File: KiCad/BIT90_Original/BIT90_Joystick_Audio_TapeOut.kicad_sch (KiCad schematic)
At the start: 21 parts, among them U10 74LS04, U11 74LS138, U12 74LS00, U14 74LS05, U25 LM393, U33 74LS244, U34 74LS244, U6 SN76489AN, U9 74LS00

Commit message: Minor schematic corrections
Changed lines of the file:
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@@
 		(company "Brett Hallen")
 		(comment 3 "From Sheet 6-3")
-		(comment 4 "Based on original schematics from BIT Corporation")
+		(comment 4 "Based on original schematics from BIT Corporation (普澤有限公司)")
 	)
 	(text_box "I don't understand this:\nU12 pin 12 input connected to U10 pin 13 input ... ?"
@@
 	)
 	(global_label "AUDIO OUT"
-		(shape input)
+		(shape output)
 		(at 57.15 40.64 180)
 		(fields_autoplaced yes)

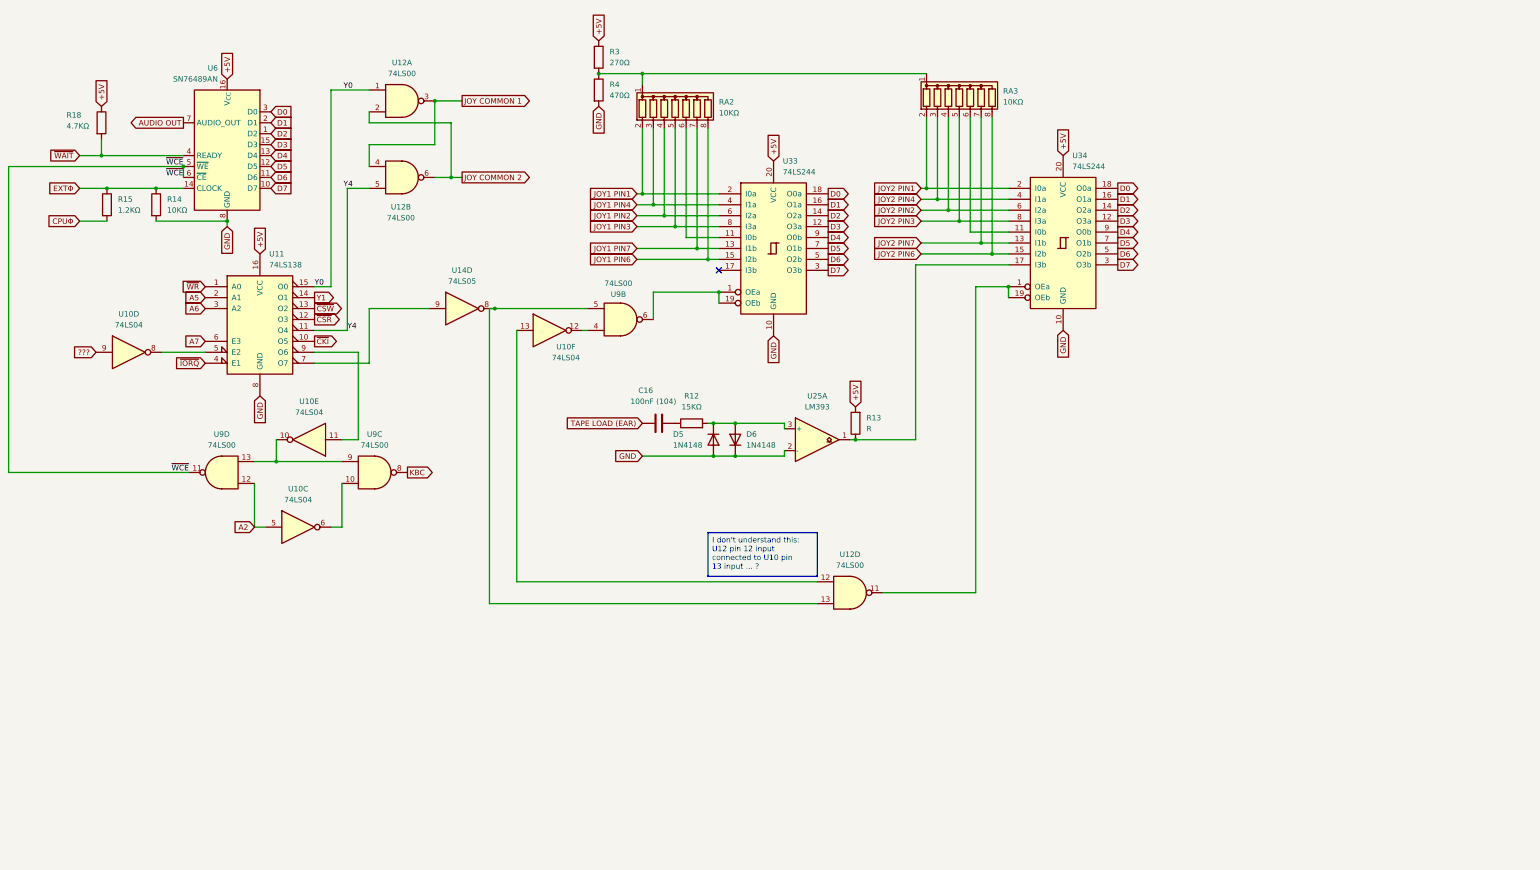
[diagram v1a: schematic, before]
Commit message: Completed original schematic redraw
Well, didn't finish the Video Encoder (PAL) sheet as I'm not going to use any of it in the new design.
Moved the audio output from that sheet to the Joystick/Audio/Tape out sheet where the sound generator is.
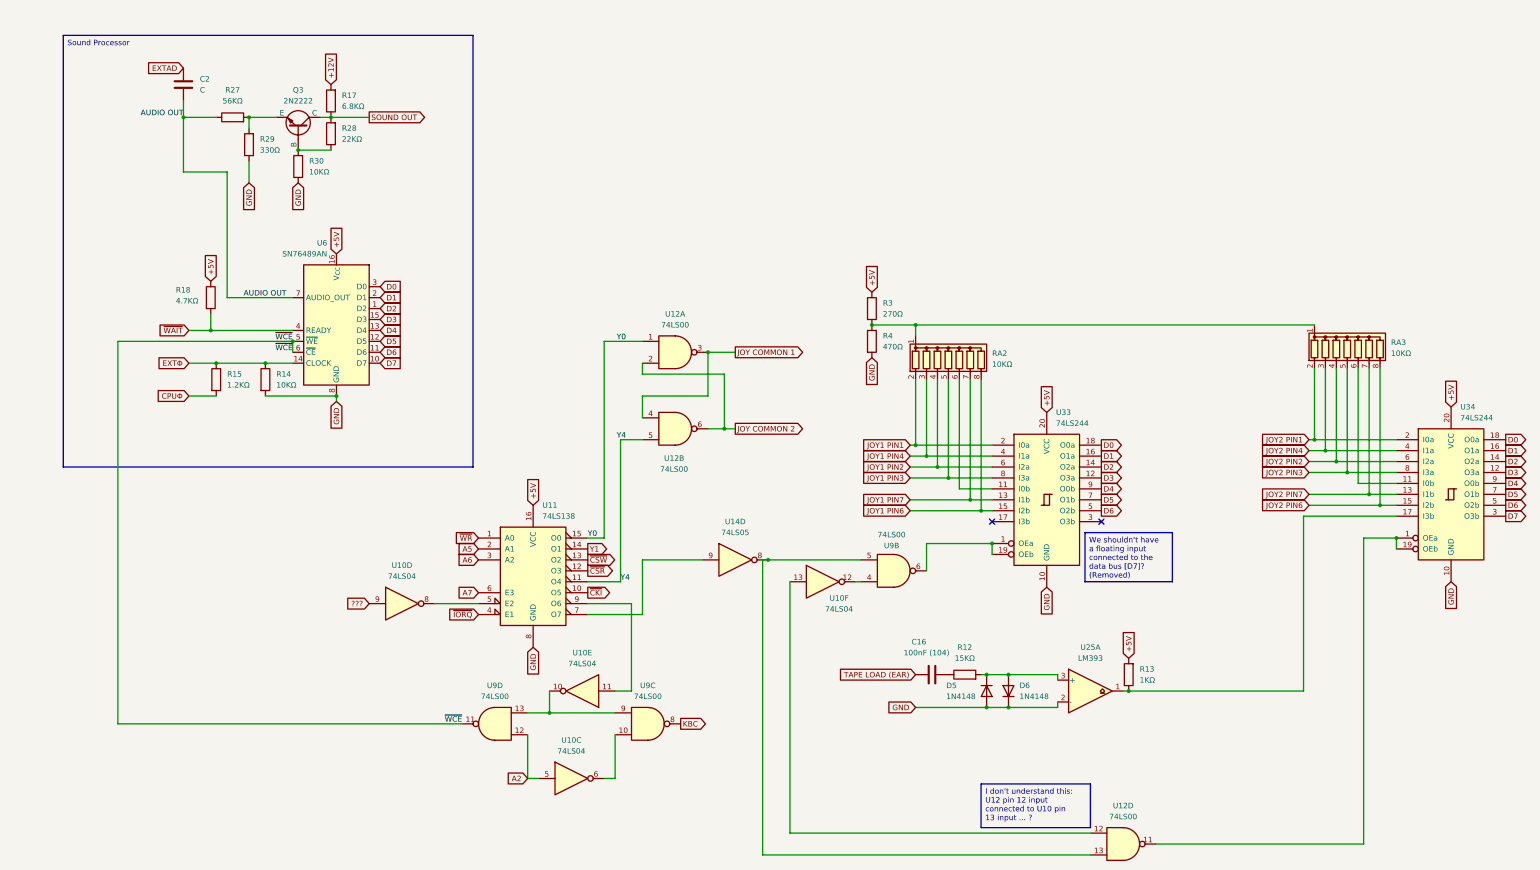
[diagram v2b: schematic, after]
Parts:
- added C2: C, symbol Device:C
- added Q3: 2N2222, symbol Simulation_SPICE:NPN
- added R17: 6.8KΩ, symbol Device:R
- added R27: 56KΩ, symbol Device:R
- added R28: 22KΩ, symbol Device:R
- added R29: 330Ω, symbol Device:R
- added R30: 10KΩ, symbol Device:R
- R13: value R -> 1KΩ
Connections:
- net AUDIO OUT: now also C2.2, R27.1
- net D7: no longer U33.3 (O3b)
- net GND: now also R29.1, R30.1
- new net: Q3.3 (E), R27.2, R29.2
- new net: Q3.2 (B), R28.1, R30.2
- new net +12V: R17.2
- new net EXTAD: C2.1
- new net SOUND OUT: Q3.1 (C), R17.1, R28.2
- no-connect marks 1 -> 2
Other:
- moved on the sheet: C16, D5, D6, R12, R13, R14, R15, R18, R3, R4, RA2, RA3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

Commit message: Small updates/corrections
Managed to figure out some more errors/missing info from ColecoVision schematics & Henk's BIT90 motherboard underside photo
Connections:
- net D7: now also U33.3 (O3b)
- net A1: now reaches U10.13, U12.12
- net ??? renamed ~{DISM}
- net JOY COMMON 1 renamed CTRL COMMON 1
- net JOY COMMON 2 renamed CTRL COMMON 2
- net JOY1 PIN1 renamed CTRL1 PIN1
- net JOY1 PIN2 renamed CTRL1 PIN2
- net JOY1 PIN3 renamed CTRL1 PIN3
- net JOY1 PIN4 renamed CTRL1 PIN4
- net JOY1 PIN6 renamed CTRL1 PIN6
- net JOY1 PIN7 renamed CTRL1 PIN7
- net JOY2 PIN1 renamed CTRL2 PIN1
- net JOY2 PIN2 renamed CTRL2 PIN2
- net JOY2 PIN3 renamed CTRL2 PIN3
- net JOY2 PIN4 renamed CTRL2 PIN4
- net JOY2 PIN6 renamed CTRL2 PIN6
- net JOY2 PIN7 renamed CTRL2 PIN7
- no-connect marks 2 -> 1
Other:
- moved on the sheet: U10F, U12D, U9B
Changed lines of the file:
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@@
 	(title_block
 		(title "BIT90 Joystick, Audio, Tape Out")
-		(date "3/JUN/2026")
+		(date "5/JUN/2026")
 		(rev "A")
 		(company "Brett Hallen")
@@
 		(comment 4 "Based on original schematics from BIT Corporation (普澤有限公司)")
 	)
-	(text_box "I don't understand this:\nU12 pin 12 input connected to U10 pin 13 input ... ?"
+	(text_box "Sound Processor"
 		(exclude_from_sim no)
-		(at 242.57 194.31 0)
-		(size 25.4 10.16)
+		(at 29.21 20.32 0)
+		(size 95.25 100.33)
 		(margins 0.9525 0.9525 0.9525 0.9525)
 		(stroke
@@
 		)
 	)
-	(text_box "Sound Processor"
+	(text_box "We shouldn't have a floating input connected to the data bus [D7]?"
 		(exclude_from_sim no)
-		(at 29.21 20.32 0)
-		(size 95.25 100.33)
+		(at 267.97 137.16 0)
+		(size 20.32 10.16)
 		(margins 0.9525 0.9525 0.9525 0.9525)
 		(stroke
@@
 		)
 	)
-	(text_box "We shouldn't have a floating input connected to the data bus [D7]? (Removed)"
+	(text_box "Inverter input is unlabelled on the original BIT90 schematic.\nIt comes from pin 29 on the expansion connector in the ColecoVision so assuming same here "
 		(exclude_from_sim no)
-		(at 266.7 135.89 0)
-		(size 20.32 11.43)
+		(at 66.04 154.94 0)
+		(size 34.29 15.24)
 		(margins 0.9525 0.9525 0.9525 0.9525)
 		(stroke
@@
 		(at 245.11 133.35)
 	)
-	(no_connect
-		(at 270.51 133.35)
-	)
 	(wire
 		(pts
-			(xy 245.11 138.43) (xy 229.87 138.43)
+			(xy 245.11 138.43) (xy 233.68 138.43)
 		)
 		(stroke
@@
 	(wire
 		(pts
-			(xy 331.47 208.28) (xy 283.21 208.28)
+			(xy 331.47 191.77) (xy 237.49 191.77)
 		)
 		(stroke
@@
 	(wire
 		(pts
-			(xy 331.47 208.28) (xy 331.47 137.16)
+			(xy 331.47 191.77) (xy 331.47 137.16)
 		)
 		(stroke
@@
 	(wire
 		(pts
-			(xy 213.36 147.32) (xy 214.63 147.32)
-		)
-		(stroke
-			(width 0)
-			(type default)
-		)
-	)
-	(wire
-		(pts
 			(xy 58.42 96.52) (xy 64.77 96.52)
 		)
@@
 	(wire
 		(pts
-			(xy 267.97 210.82) (xy 191.77 210.82)
+			(xy 222.25 194.31) (xy 193.04 194.31)
 		)
 		(stroke
@@
 	(wire
 		(pts
-			(xy 229.87 138.43) (xy 229.87 144.78)
+			(xy 233.68 138.43) (xy 233.68 144.78)
 		)
 		(stroke
@@
 	(wire
 		(pts
-			(xy 193.04 142.24) (xy 214.63 142.24)
+			(xy 193.04 142.24) (xy 218.44 142.24)
 		)
 		(stroke
@@
 	(wire
 		(pts
-			(xy 198.12 147.32) (xy 198.12 205.74)
-		)
-		(stroke
-			(width 0)
-			(type default)
-		)
-	)
-	(wire
-		(pts
 			(xy 63.5 88.9) (xy 82.55 88.9)
 		)
@@
 	(wire
 		(pts
-			(xy 191.77 210.82) (xy 191.77 142.24)
+			(xy 193.04 194.31) (xy 193.04 142.24)
 		)
 		(stroke
@@
 	(wire
 		(pts
-			(xy 198.12 205.74) (xy 267.97 205.74)
-		)
-		(stroke
-			(width 0)
-			(type default)
-		)
-	)
-	(wire
-		(pts
-			(xy 193.04 142.24) (xy 191.77 142.24)
-		)
-		(stroke
-			(width 0)
-			(type default)
-		)
-	)
-	(wire
-		(pts
 			(xy 234.95 100.33) (xy 234.95 123.19)
 		)
@@
 		)
 	)
-	(global_label "???"
+	(global_label "~{DISM}"
 		(shape input)
 		(at 100.33 152.4 180)
@@
 		)
 		(property "Intersheetrefs" "${INTERSHEET_REFS}"
-			(at 94.079 152.4 0)
+			(at 92.8091 152.4 0)
 			(effects
 				(font
@@
 		)
 	)
-	(global_label "JOY2 PIN7"
+	(global_label "CTRL2 PIN7"
 		(shape input)
 		(at 318.77 127 180)
@@
 		)
 	)
+	(global_label "A1"
+		(shape input)
+		(at 222.25 189.23 180)
+		(fields_autoplaced yes)
+		(effects
+			(font
+				(size 1.27 1.27)
+			)
+			(justify right)
+		)
+		(property "Intersheetrefs" "${INTERSHEET_REFS}"
+			(at 216.9667 189.23 0)
+			(effects
+				(font
+					(size 1.27 1.27)
+				)
+				(justify right)
+				(hide yes)
+			)
+		)
+	)
 	(global_label "D3"
 		(shape output)
@@
 		)
 	)
-	(global_label "JOY1 PIN6"
+	(global_label "CTRL1 PIN6"
 		(shape input)
 		(at 226.06 130.81 180)
@@
 		)
 	)
-	(global_label "JOY1 PIN1"
+	(global_label "CTRL1 PIN1"
 		(shape input)
 		(at 226.06 115.57 180)
@@
 		)
 	)
-	(global_label "JOY2 PIN3"
+	(global_label "CTRL2 PIN3"
 		(shape input)
 		(at 318.77 121.92 180)
@@
 		)
 	)
-	(global_label "JOY2 PIN4"
+	(global_label "CTRL2 PIN4"
 		(shape input)
 		(at 318.77 116.84 180)
@@
 		)
 	)
+	(global_label "A1"
+		(shape input)
+		(at 203.2 147.32 180)
+		(fields_autoplaced yes)
+		(effects
+			(font
+				(size 1.27 1.27)
+			)
+			(justify right)
+		)
+		(property "Intersheetrefs" "${INTERSHEET_REFS}"
+			(at 197.9167 147.32 0)
+			(effects
+				(font
+					(size 1.27 1.27)
+				)
+				(justify right)
+				(hide yes)
+			)
+		)
+	)
 	(global_label "D7"
 		(shape output)
@@
 		)
 	)
-	(global_label "JOY2 PIN2"
+	(global_label "CTRL2 PIN2"
 		(shape input)
 		(at 318.77 119.38 180)
@@
 		)
 	)
-	(global_label "JOY COMMON 1"
+	(global_label "CTRL COMMON 1"
 		(shape output)
 		(at 185.42 93.98 0)
@@
 		)
 	)
-	(global_label "JOY1 PIN7"
+	(global_label "CTRL1 PIN7"
 		(shape input)
 		(at 226.06 128.27 180)
@@
 		)
 	)
-	(global_label "JOY2 PIN6"
+	(global_label "CTRL2 PIN6"
 		(shape input)
 		(at 318.77 129.54 180)
@@
 		)
 	)
+	(global_label "D7"
+		(shape output)
+		(at 270.51 133.35 0)
+		(fields_autoplaced yes)
+		(effects
+			(font
+				(size 1.27 1.27)
+			)
+			(justify left)
+		)
+		(property "Intersheetrefs" "${INTERSHEET_REFS}"
+			(at 275.9747 133.35 0)
+			(effects
+				(font
+					(size 1.27 1.27)
+				)
+				(justify left)
+				(hide yes)
+			)
+		)
+	)
 	(global_label "~{CKI}"
 		(shape output)
@@
 		)
 	)
-	(global_label "JOY1 PIN2"
+	(global_label "CTRL1 PIN2"
 		(shape input)
 		(at 226.06 120.65 180)
@@
 		)
 	)
-	(global_label "JOY COMMON 2"
+	(global_label "CTRL COMMON 2"
 		(shape output)
 		(at 185.42 111.76 0)
@@
 		)
 	)
-	(global_label "JOY2 PIN1"
+	(global_label "CTRL2 PIN1"
 		(shape input)
 		(at 318.77 114.3 180)
@@
 		)
 	)
-	(global_label "JOY1 PIN4"
+	(global_label "CTRL1 PIN4"
 		(shape input)
 		(at 226.06 118.11 180)
@@
 		)
 	)
-	(global_label "JOY1 PIN3"
+	(global_label "CTRL1 PIN3"
 		(shape input)
 		(at 226.06 123.19 180)
@@
 	(symbol
 		(lib_id "74xx:74LS00")
-		(at 275.59 208.28 0)
+		(at 229.87 191.77 0)
 		(unit 4)
 		(exclude_from_sim no)
@@
 		(fields_autoplaced yes)
 		(property "Reference" "U12"
-			(at 275.5817 199.39 0)
+			(at 229.8617 182.88 0)
 			(effects
 				(font
@@
 		)
 		(property "Value" "74LS00"
-			(at 275.5817 201.93 0)
+			(at 229.8617 185.42 0)
 			(effects
 				(font
@@
 		)
 		(property "Footprint" ""
-			(at 275.59 208.28 0)
+			(at 229.87 191.77 0)
 			(effects
 				(font
@@
 		)
 		(property "Datasheet" "http://www.ti.com/lit/gpn/sn74ls00"
-			(at 275.59 208.28 0)
+			(at 229.87 191.77 0)
 			(effects
 				(font
@@
 		)
 		(property "Description" "quad 2-input NAND gate"
-			(at 275.59 208.28 0)
+			(at 229.87 191.77 0)
 			(effects
 				(font
@@
 	(symbol
 		(lib_id "74xx:74LS00")
-		(at 222.25 144.78 0)
+		(at 226.06 144.78 0)
 		(mirror x)
 		(unit 2)
@@
 		(dnp no)
 		(property "Reference" "U9"
-			(at 221.742 138.938 0)
+			(at 225.552 138.938 0)
 			(effects
 				(font
@@
 		)
 		(property "Value" "74LS00"
-			(at 221.742 136.398 0)
+			(at 225.552 136.398 0)
 			(effects
 				(font
@@
 		)
 		(property "Footprint" ""
-			(at 222.25 144.78 0)
+			(at 226.06 144.78 0)
 			(effects
 				(font
@@
 		)
 		(property "Datasheet" "http://www.ti.com/lit/gpn/sn74ls00"
-			(at 222.25 144.78 0)
+			(at 226.06 144.78 0)
 			(effects
 				(font
@@
 		)
 		(property "Description" "quad 2-input NAND gate"
-			(at 222.25 144.78 0)
+			(at 226.06 144.78 0)
 			(effects
 				(font
@@
 	(symbol
 		(lib_id "74xx:74LS04")
-		(at 205.74 147.32 0)
+		(at 210.82 147.32 0)
 		(unit 6)
 		(exclude_from_sim no)
@@
 		(dnp no)
 		(property "Reference" "U10"
-			(at 209.55 151.13 0)
+			(at 214.63 151.13 0)
 			(effects
 				(font
@@
 		)
 		(property "Value" "74LS04"
-			(at 209.55 153.67 0)
+			(at 214.63 153.67 0)
 			(effects
 				(font
@@
 		)
 		(property "Footprint" ""
-			(at 205.74 147.32 0)
+			(at 210.82 147.32 0)
 			(effects
 				(font
@@
 		)
 		(property "Datasheet" "http://www.ti.com/lit/gpn/sn74LS04"
-			(at 205.74 147.32 0)
+			(at 210.82 147.32 0)
 			(effects
 				(font
@@
 		)
 		(property "Description" "Hex Inverter"
-			(at 205.74 147.32 0)
+			(at 210.82 147.32 0)
 			(effects
 				(font

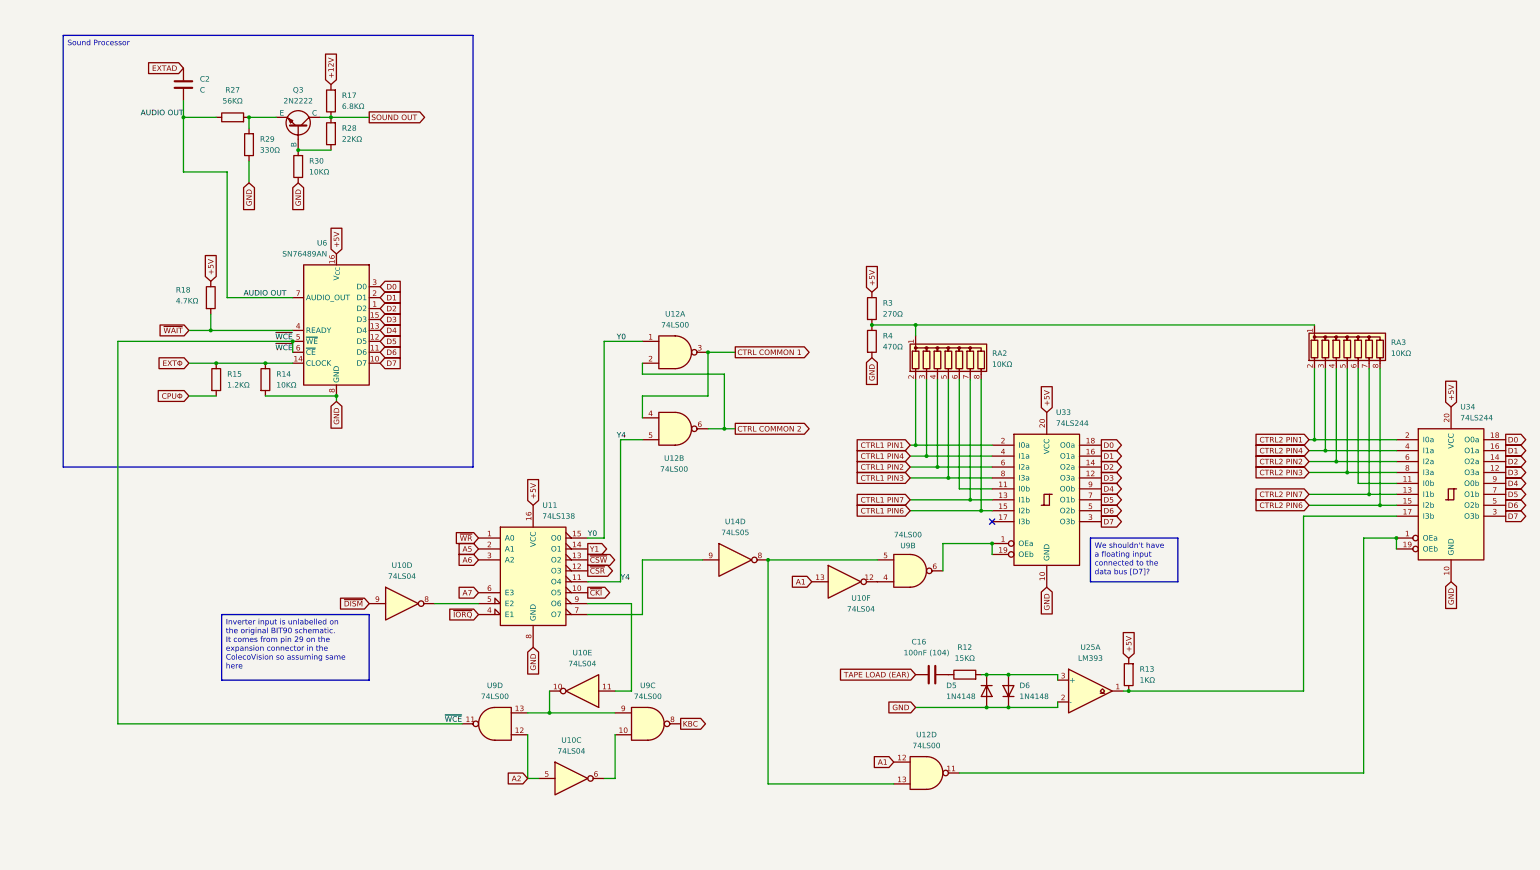
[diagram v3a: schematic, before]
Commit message: Resolved audio clock signal
Marked as EXTΦ on BIT90 schematic, generated via resistor from CPUΦ
Renamed it as AUDΦ so it's a bit clearer
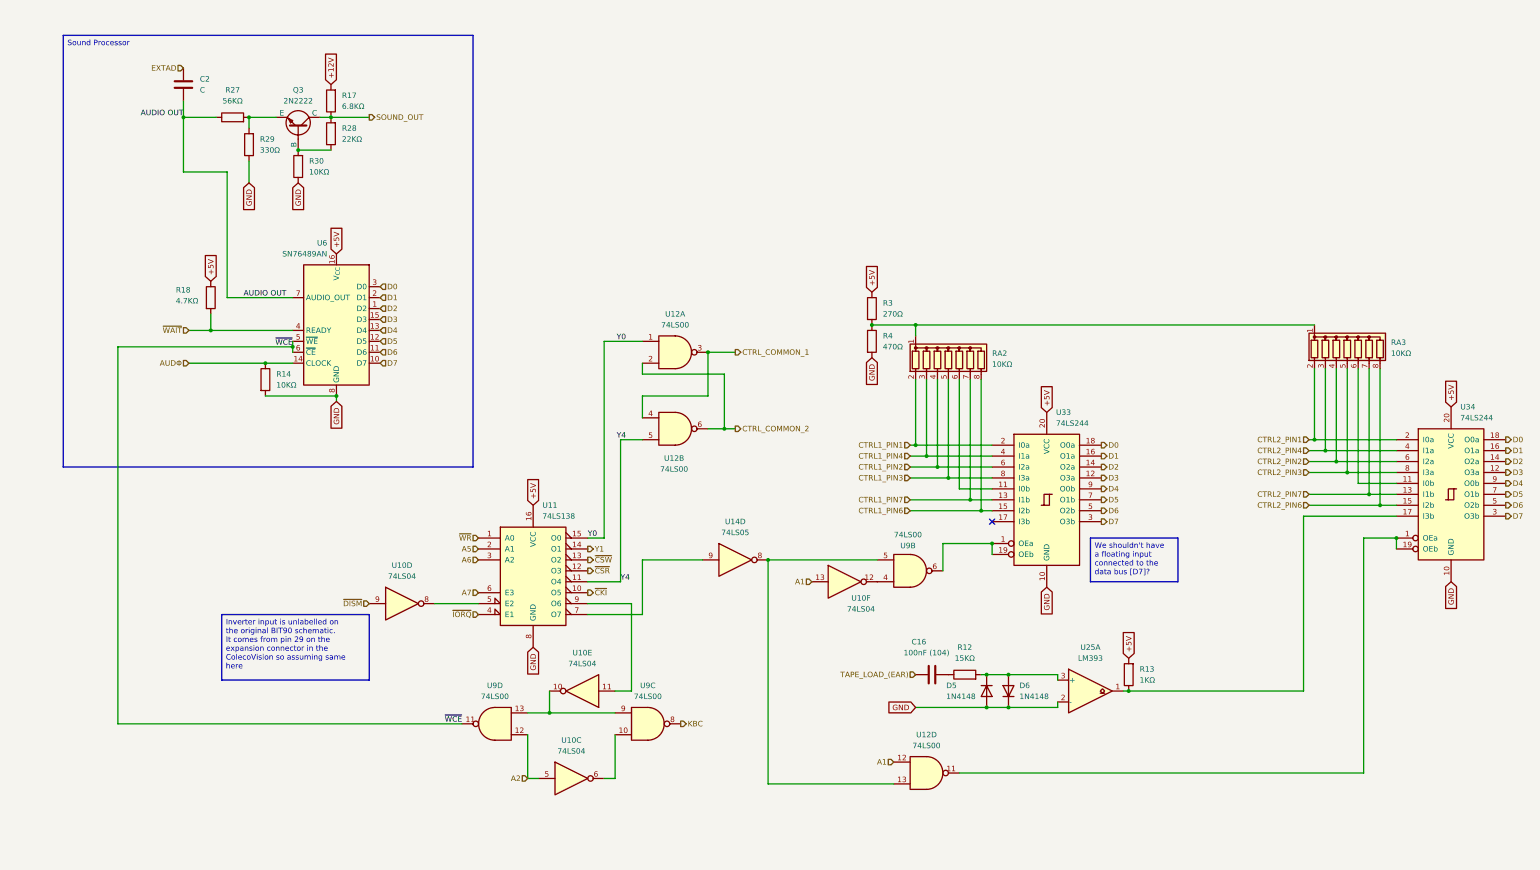
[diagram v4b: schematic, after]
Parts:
- removed R15: 1.2KΩ, symbol Device:R
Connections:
- net CTRL COMMON 1 renamed CTRL_COMMON_1
- net CTRL COMMON 2 renamed CTRL_COMMON_2
- net CTRL1 PIN1 renamed CTRL1_PIN1
- net CTRL1 PIN2 renamed CTRL1_PIN2
- net CTRL1 PIN3 renamed CTRL1_PIN3
- net CTRL1 PIN4 renamed CTRL1_PIN4
- net CTRL1 PIN6 renamed CTRL1_PIN6
- net CTRL1 PIN7 renamed CTRL1_PIN7
- net CTRL2 PIN1 renamed CTRL2_PIN1
- net CTRL2 PIN2 renamed CTRL2_PIN2
- net CTRL2 PIN3 renamed CTRL2_PIN3
- net CTRL2 PIN4 renamed CTRL2_PIN4
- net CTRL2 PIN6 renamed CTRL2_PIN6
- net CTRL2 PIN7 renamed CTRL2_PIN7
- net EXTΦ renamed AUDΦ
- net SOUND OUT renamed SOUND_OUT
- net TAPE LOAD (EAR) renamed TAPE_LOAD_(EAR)

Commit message: Minor corrections
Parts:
- C2: value C -> 102?
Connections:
- net AUDIO OUT renamed AUDIO_OUT
- net ~{DISM} renamed ~{DISIO}
